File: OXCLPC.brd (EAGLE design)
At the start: 49.5 x 18 mm, 5 parts

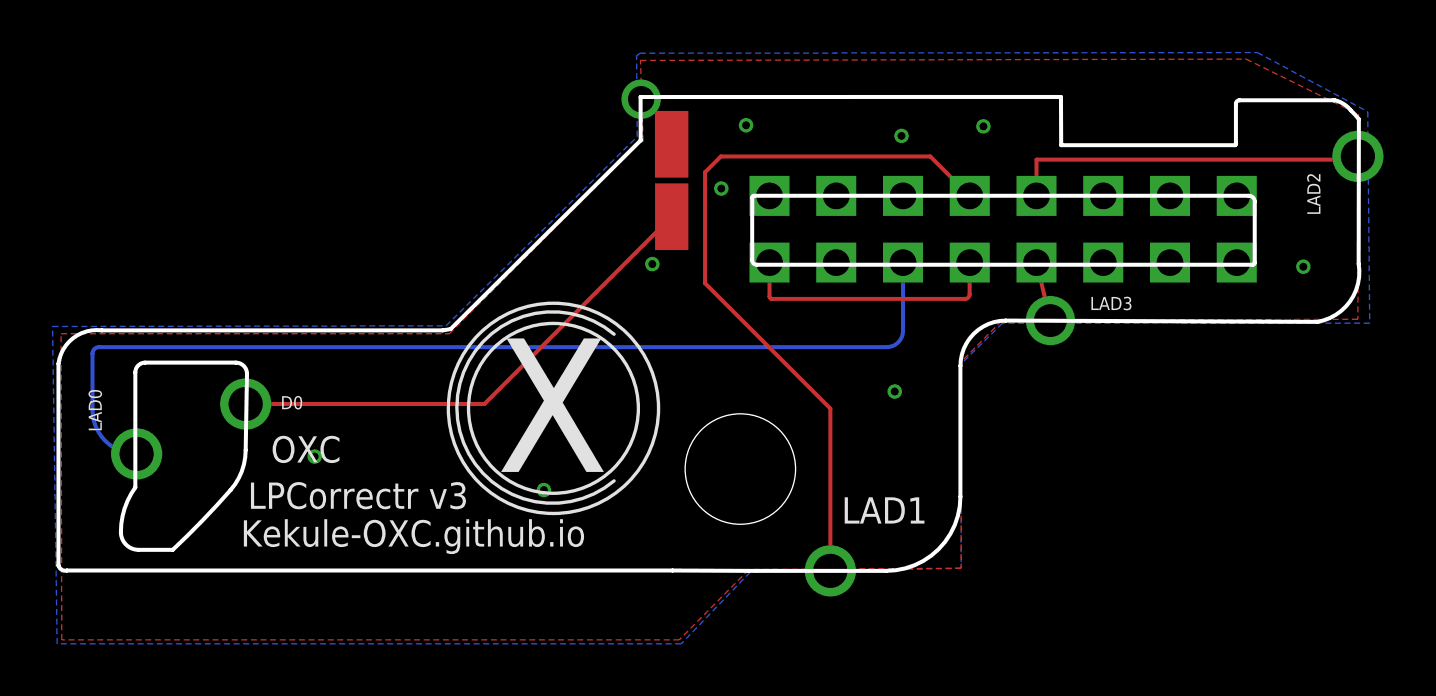
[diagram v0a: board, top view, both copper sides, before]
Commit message: changed GND hole to appease the pcb manufacturers
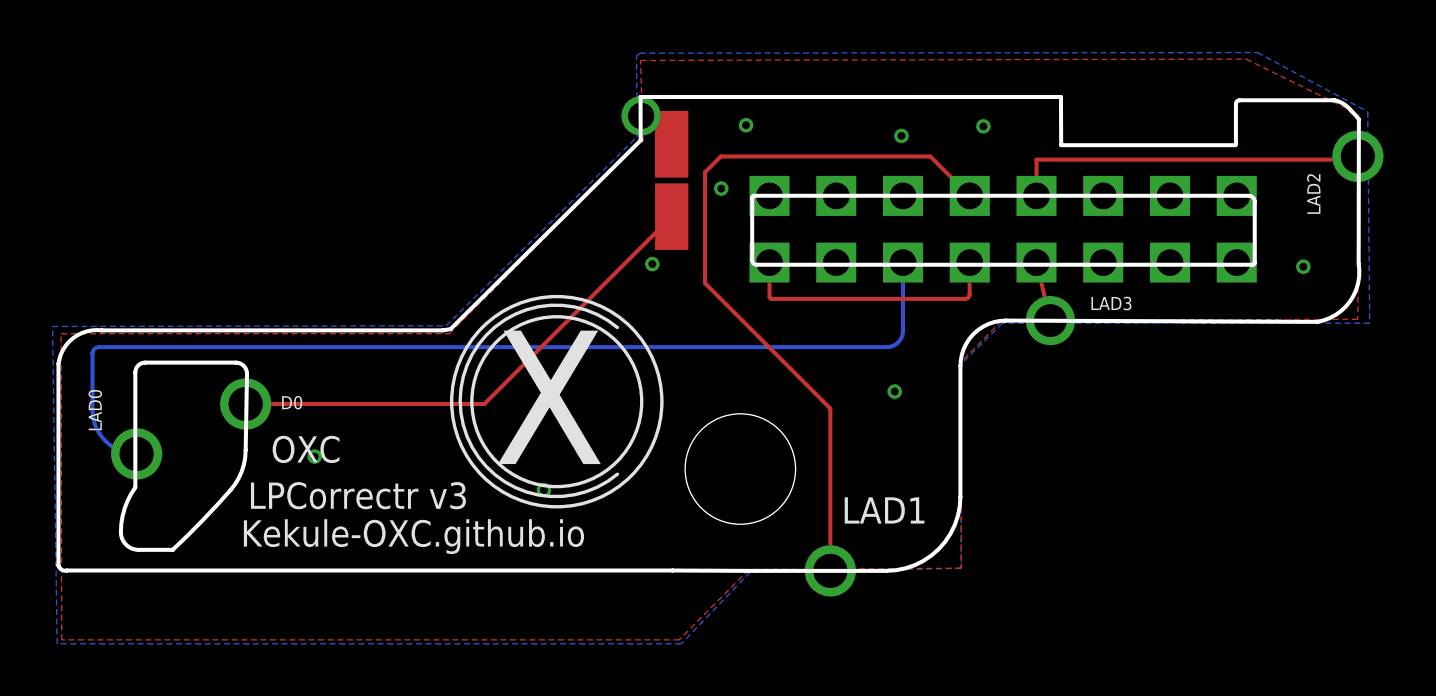
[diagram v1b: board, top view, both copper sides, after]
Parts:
- moved U$2 0.28 mm to (1.40, -18.3)
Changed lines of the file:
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@@
 </element>
 <element name="U$1" library="adapter8784" package="TEST" value="" x="4.771" y="-22.297" smashed="yes" rot="MR0"/>
-<element name="U$2" library="OXC_Library" package="OXC_NO_TM" value="" x="1.27" y="-18.542" smashed="yes"/>
+<element name="U$2" library="OXC_Library" package="OXC_NO_TM" value="" x="1.397" y="-18.288" smashed="yes"/>
 </elements>
 <signals>
@@
 <contactref element="SV1" pad="11"/>
 <via x="-14.575" y="-20.575" extent="1-16" drill="1.3" shape="square" locked="yes"/>
-<wire x1="14.59" y1="-13.295" x2="14.575" y2="-13.295" width="0.1524" layer="16"/>
 <wire x1="-14.575" y1="-20.575" x2="-16.256" y2="-18.894" width="0.1524" layer="16" curve="-90"/>
 <wire x1="-16.256" y1="-18.894" x2="-16.256" y2="-16.764" width="0.1524" layer="16"/>
@@
 </signal>
 <signal name="N$1">
-<via x="4.625" y="-7.075" extent="1-16" drill="1" shape="square"/>
+<via x="4.625" y="-7.71" extent="1-16" drill="1" shape="square"/>
 </signal>
 </signals>

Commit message: Add files via upload
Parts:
- removed U$2: (no value), OXC_Library:OXC_NO_TM
- added U$3: (no value), OXC_Library:OXC_NO_TM
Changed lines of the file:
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@@
 </element>
 <element name="U$1" library="adapter8784" package="TEST" value="" x="4.771" y="-22.297" smashed="yes" rot="MR0"/>
-<element name="U$2" library="OXC_Library" package="OXC_NO_TM" value="" x="1.397" y="-18.288" smashed="yes"/>
+<element name="U$3" library="OXC_Library" package="OXC_NO_TM" value="" x="1.397" y="-18.542" smashed="yes"/>
 </elements>
 <signals>
@@
 </signal>
 <signal name="N$1">
-<via x="4.625" y="-7.71" extent="1-16" drill="1" shape="square"/>
+<via x="4.625" y="-7.964" extent="1-16" drill="1.3" shape="square"/>
 </signal>
 </signals>
